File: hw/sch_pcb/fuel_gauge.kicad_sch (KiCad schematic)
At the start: 35 parts, among them P1 HEADER_2x05_PARALLEL, SW1 SW_PUSH, U1 BQ34Z100, U2 SN74HC164D

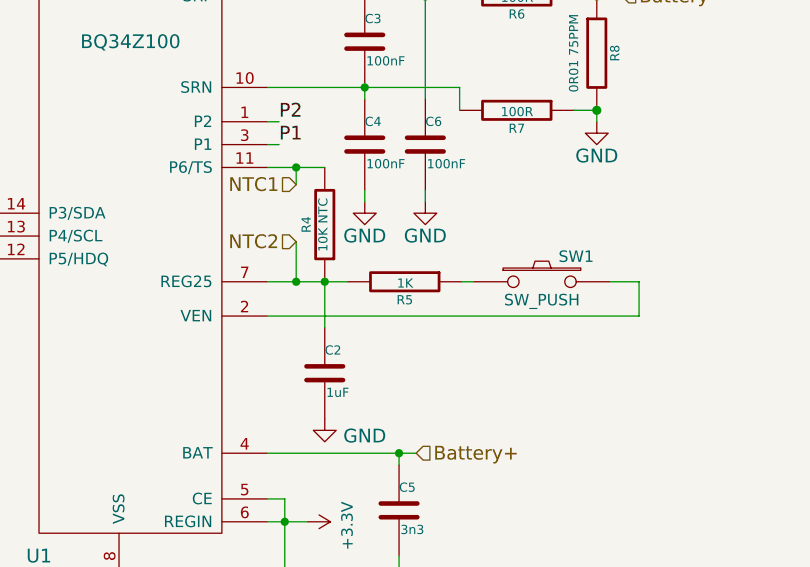
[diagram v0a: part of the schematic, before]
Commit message: Edit UST ID
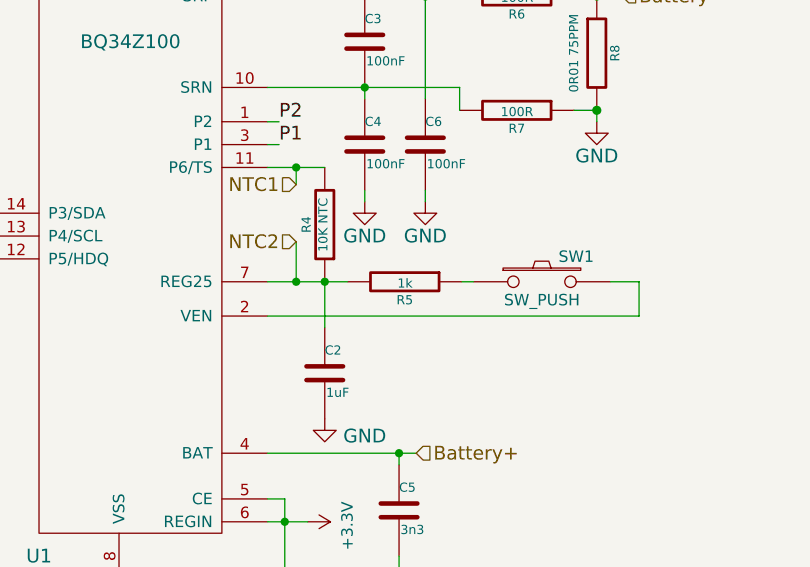
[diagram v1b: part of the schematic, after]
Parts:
- C1, C3, C4, C6, C7: UST_ID (none) -> 5c70984712875079b91f8b4c
- C2: UST_ID (none) -> 5c70984712875079b91f8b50
- C5: UST_ID (none) -> 5c70984712875079b91f8b47
- D1, D2, D3, D4, D5, D6, D7, D8: UST_ID (none) -> 5c70984412875079b91f8897
- R1, R2, R3: UST_ID (none) -> 5e3ffaff1287502a33bad825
- R10, R11, R12, R13, R14, R15, R16, R9: UST_ID (none) -> 5c70984512875079b91f8983
- R4: UST_ID (none) -> 5c70984712875079b91f8ac5
- R5: value 1K -> 1k; UST_ID (none) -> 5c70984512875079b91f898c
- R6, R7: UST_ID (none) -> 5c70984512875079b91f8977
- R8: UST_ID (none) -> 5c70984712875079b91f8ab0
- SW1: UST_ID (none) -> 5c70984712875079b91f8ad1
- U1: UST_ID (none) -> 5c70984612875079b91f89c3
- U2: UST_ID (none) -> 5c70984612875079b91f89ed
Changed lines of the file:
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@@
       (effects (font (size 0.762 0.762)))
+    )
+    (property "UST_ID" "5c70984512875079b91f8983" (id 4) (at 227.965 110.49 0)
+      (effects (font (size 1.27 1.27)) hide)
     )
     (pin "1")
@@
       (effects (font (size 0.762 0.762)))
     )
+    (property "UST_ID" "5c70984512875079b91f8983" (id 4) (at 227.965 106.68 0)
+      (effects (font (size 1.27 1.27)) hide)
+    )
     (pin "1")
     (pin "2")
@@
       (effects (font (size 0.762 0.762)))
     )
+    (property "UST_ID" "5c70984512875079b91f8977" (id 4) (at 142.621 81.28 0)
+      (effects (font (size 1.27 1.27)) hide)
+    )
     (pin "1")
     (pin "2")
@@
       (effects (font (size 0.762 0.762)))
     )
+    (property "UST_ID" "5c70984712875079b91f8ab0" (id 4) (at 151.511 74.93 0)
+      (effects (font (size 1.27 1.27)) hide)
+    )
     (pin "1")
     (pin "2")
@@
     (property "Datasheet" "https://www.ti.com/lit/ds/symlink/bq34z100-g1.pdf" (id 3) (at 103.505 85.09 0)
       (effects (font (size 1.524 1.524)) hide)
+    )
+    (property "UST_ID" "5c70984612875079b91f89c3" (id 4) (at 98.425 83.82 0)
+      (effects (font (size 1.27 1.27)) hide)
     )
     (pin "1")
@@
       (effects (font (size 1.524 1.524)))
     )
+    (property "UST_ID" "5c70984412875079b91f8897" (id 4) (at 241.935 87.63 0)
+      (effects (font (size 1.27 1.27)) hide)
+    )
     (pin "1")
     (pin "2")
@@
       (effects (font (size 1.524 1.524)))
     )
+    (property "UST_ID" "5c70984712875079b91f8b50" (id 4) (at 121.285 110.49 0)
+      (effects (font (size 1.27 1.27)) hide)
+    )
     (pin "1")
     (pin "2")
@@
       (effects (font (size 1.524 1.524)))
     )
+    (property "UST_ID" "5c70984412875079b91f8897" (id 4) (at 241.935 83.82 0)
+      (effects (font (size 1.27 1.27)) hide)
+    )
     (pin "1")
     (pin "2")
@@
       (effects (font (size 0.762 0.762)))
     )
+    (property "UST_ID" "5e3ffaff1287502a33bad825" (id 4) (at 73.66 81.28 0)
+      (effects (font (size 1.27 1.27)) hide)
+    )
     (pin "1")
     (pin "2")
@@
       (effects (font (size 0.762 0.762)))
     )
+    (property "UST_ID" "5c70984512875079b91f8983" (id 4) (at 227.965 91.44 0)
+      (effects (font (size 1.27 1.27)) hide)
+    )
     (pin "1")
     (pin "2")
@@
       (effects (font (size 1.524 1.524)))
     )
+    (property "UST_ID" "5c70984712875079b91f8b4c" (id 4) (at 125.73 73.66 0)
+      (effects (font (size 1.27 1.27)) hide)
+    )
     (pin "1")
     (pin "2")
@@
       (effects (font (size 1.524 1.524)))
     )
+    (property "UST_ID" "5c70984712875079b91f8b47" (id 4) (at 129.54 125.73 0)
+      (effects (font (size 1.27 1.27)) hide)
+    )
     (pin "1")
     (pin "2")
@@
     (property "Datasheet" "" (id 3) (at 116.84 137.16 0)
       (effects (font (size 1.524 1.524)))
+    )
+    (property "UST_ID" "5c70984712875079b91f8b4c" (id 4) (at 116.84 137.16 0)
+      (effects (font (size 1.27 1.27)) hide)
     )
     (pin "1")
@@
       (effects (font (size 1.524 1.524)))
     )
+    (property "UST_ID" "5c70984412875079b91f8897" (id 4) (at 241.935 102.87 0)
+      (effects (font (size 1.27 1.27)) hide)
+    )
     (pin "1")
     (pin "2")
@@
       (effects (font (size 1.524 1.524)))
     )
+    (property "UST_ID" "5c70984412875079b91f8897" (id 4) (at 241.935 95.25 0)
+      (effects (font (size 1.27 1.27)) hide)
+    )
     (pin "1")
     (pin "2")
@@
       (effects (font (size 1.524 1.524)))
     )
+    (property "UST_ID" "5c70984412875079b91f8897" (id 4) (at 241.935 106.68 0)
+      (effects (font (size 1.27 1.27)) hide)
+    )
     (pin "1")
     (pin "2")
@@
     (property "Datasheet" "" (id 3) (at 125.73 85.09 0)
       (effects (font (size 1.524 1.524)))
+    )
+    (property "UST_ID" "5c70984712875079b91f8b4c" (id 4) (at 125.73 85.09 0)
+      (effects (font (size 1.27 1.27)) hide)
     )
     (pin "1")
@@
       (effects (font (size 1.016 1.016)))
     )
-    (property "Value" "1K" (id 1) (at 130.2004 100.5078 90)
+    (property "Value" "1k" (id 1) (at 130.2004 100.5078 90)
       (effects (font (size 1.016 1.016)))
     )
@@
       (effects (font (size 0.762 0.762)))
     )
+    (property "UST_ID" "5c70984512875079b91f898c" (id 4) (at 130.175 100.33 0)
+      (effects (font (size 1.27 1.27)) hide)
+    )
     (pin "1")
     (pin "2")
@@
     (property "Datasheet" "" (id 3) (at 227.965 99.06 0)
       (effects (font (size 0.762 0.762)))
+    )
+    (property "UST_ID" "5c70984512875079b91f8983" (id 4) (at 227.965 99.06 0)
+      (effects (font (size 1.27 1.27)) hide)
     )
     (pin "1")
@@
       (effects (font (size 1.524 1.524)))
     )
+    (property "UST_ID" "5c70984412875079b91f8897" (id 4) (at 241.935 91.44 0)
+      (effects (font (size 1.27 1.27)) hide)
+    )
     (pin "1")
     (pin "2")
@@
       (effects (font (size 0.762 0.762)))
     )
+    (property "UST_ID" "5e3ffaff1287502a33bad825" (id 4) (at 83.82 81.28 0)
+      (effects (font (size 1.27 1.27)) hide)
+    )
     (pin "1")
     (pin "2")
@@
     (property "Datasheet" "" (id 3) (at 207.645 100.33 0)
       (effects (font (size 1.524 1.524)))
+    )
+    (property "UST_ID" "5c70984612875079b91f89ed" (id 4) (at 202.565 99.06 0)
+      (effects (font (size 1.27 1.27)) hide)
     )
     (pin "1")
@@
       (effects (font (size 1.524 1.524)))
     )
+    (property "UST_ID" "5c70984412875079b91f8897" (id 4) (at 241.935 99.06 0)
+      (effects (font (size 1.27 1.27)) hide)
+    )
     (pin "1")
     (pin "2")
@@
     (property "Datasheet" "" (id 3) (at 241.935 110.49 0)
       (effects (font (size 1.524 1.524)))
+    )
+    (property "UST_ID" "5c70984412875079b91f8897" (id 4) (at 241.935 110.49 0)
+      (effects (font (size 1.27 1.27)) hide)
     )
     (pin "1")
@@
       (effects (font (size 0.762 0.762)))
     )
+    (property "UST_ID" "5c70984512875079b91f8977" (id 4) (at 142.621 68.58 0)
+      (effects (font (size 1.27 1.27)) hide)
+    )
     (pin "1")
     (pin "2")
@@
       (effects (font (size 1.524 1.524)))
     )
+    (property "UST_ID" "5c70984712875079b91f8ad1" (id 4) (at 145.415 100.33 0)
+      (effects (font (size 1.27 1.27)) hide)
+    )
     (pin "1")
     (pin "2")
@@
     (property "Datasheet" "" (id 3) (at 227.965 87.63 0)
       (effects (font (size 0.762 0.762)))
+    )
+    (property "UST_ID" "5c70984512875079b91f8983" (id 4) (at 227.965 87.63 0)
+      (effects (font (size 1.27 1.27)) hide)
     )
     (pin "1")
@@
       (effects (font (size 0.762 0.762)))
     )
+    (property "UST_ID" "5c70984512875079b91f8983" (id 4) (at 227.965 95.25 0)
+      (effects (font (size 1.27 1.27)) hide)
+    )
     (pin "1")
     (pin "2")
@@
       (effects (font (size 0.762 0.762)))
     )
+    (property "UST_ID" "5c70984512875079b91f8983" (id 4) (at 227.965 83.82 0)
+      (effects (font (size 1.27 1.27)) hide)
+    )
     (pin "1")
     (pin "2")
@@
       (effects (font (size 1.524 1.524)))
     )
+    (property "UST_ID" "5c70984712875079b91f8b4c" (id 4) (at 132.461 85.09 0)
+      (effects (font (size 1.27 1.27)) hide)
+    )
     (pin "1")
     (pin "2")
@@
       (effects (font (size 0.762 0.762)))
     )
+    (property "UST_ID" "5c70984512875079b91f8983" (id 4) (at 227.965 102.87 0)
+      (effects (font (size 1.27 1.27)) hide)
+    )
     (pin "1")
     (pin "2")
@@
       (effects (font (size 1.524 1.524)))
     )
+    (property "UST_ID" "5c70984712875079b91f8b4c" (id 4) (at 184.785 113.03 0)
+      (effects (font (size 1.27 1.27)) hide)
+    )
     (pin "1")
     (pin "2")
@@
       (effects (font (size 0.762 0.762)))
     )
+    (property "UST_ID" "5c70984712875079b91f8ac5" (id 4) (at 121.285 93.98 0)
+      (effects (font (size 1.27 1.27)) hide)
+    )
     (pin "1")
     (pin "2")
@@
       (effects (font (size 0.762 0.762)))
     )
-    (pin "1")
+    (property "UST_ID" "5e3ffaff1287502a33bad825" (id 4) (at 78.74 81.28 0)
+      (effects (font (size 1.27 1.27)) hide)
+    )
+    (pin "1")

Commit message: Edit UST ID
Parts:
- R8: UST_ID 5c70984712875079b91f8ab0 -> 5c70984712875079b91f8abf
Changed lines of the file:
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@@
       (effects (font (size 0.762 0.762)))
     )
-    (property "UST_ID" "5c70984712875079b91f8ab0" (id 4) (at 151.511 74.93 0)
+    (property "UST_ID" "5c70984712875079b91f8abf" (id 4) (at 151.511 74.93 0)
       (effects (font (size 1.27 1.27)) hide)
     )

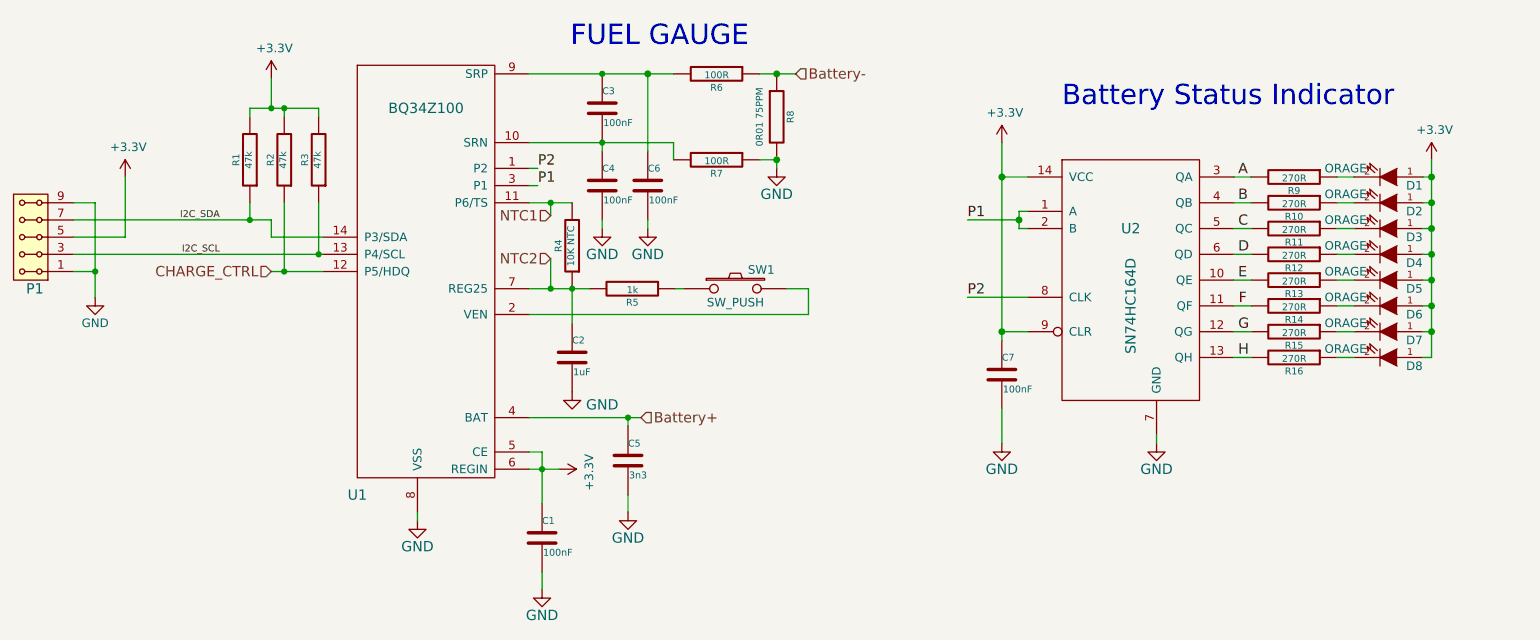
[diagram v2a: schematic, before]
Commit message: Add datasheet to the used LTO cells. Improve documentation, update KiCAD project.
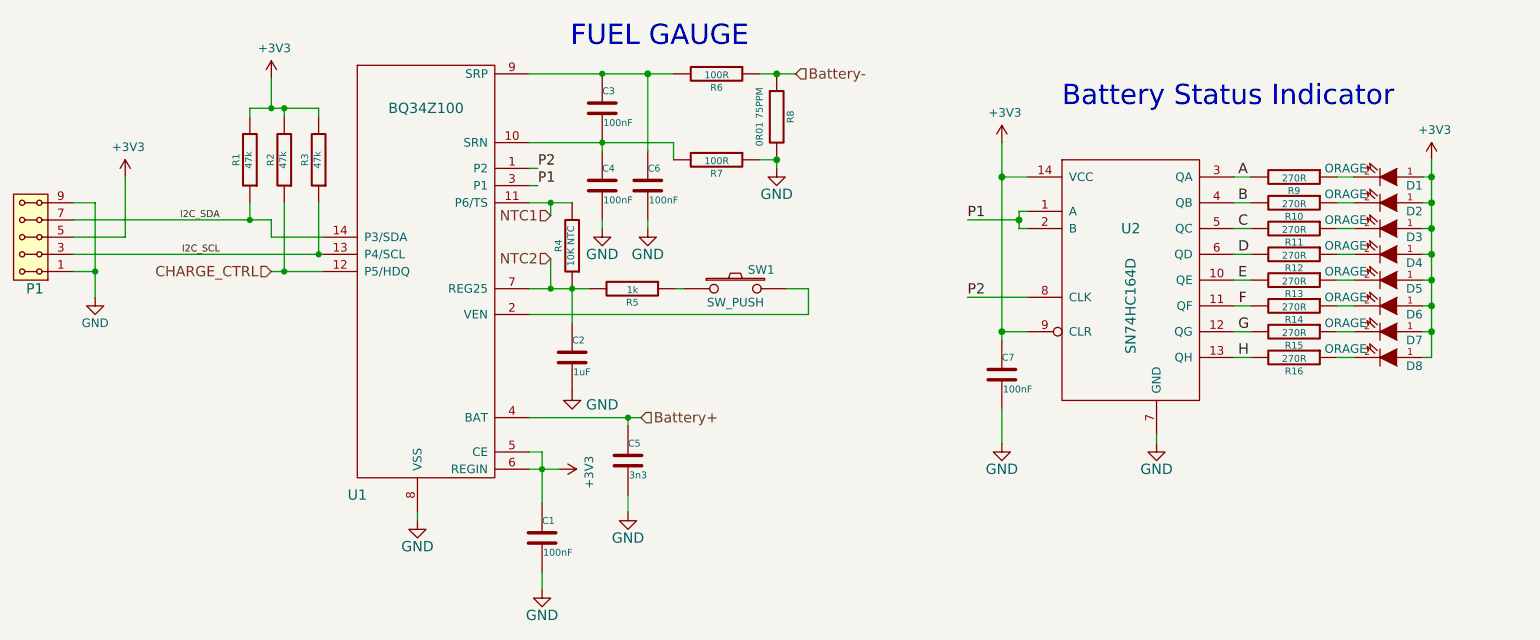
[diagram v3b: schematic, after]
